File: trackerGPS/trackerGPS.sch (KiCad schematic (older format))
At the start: 0 parts

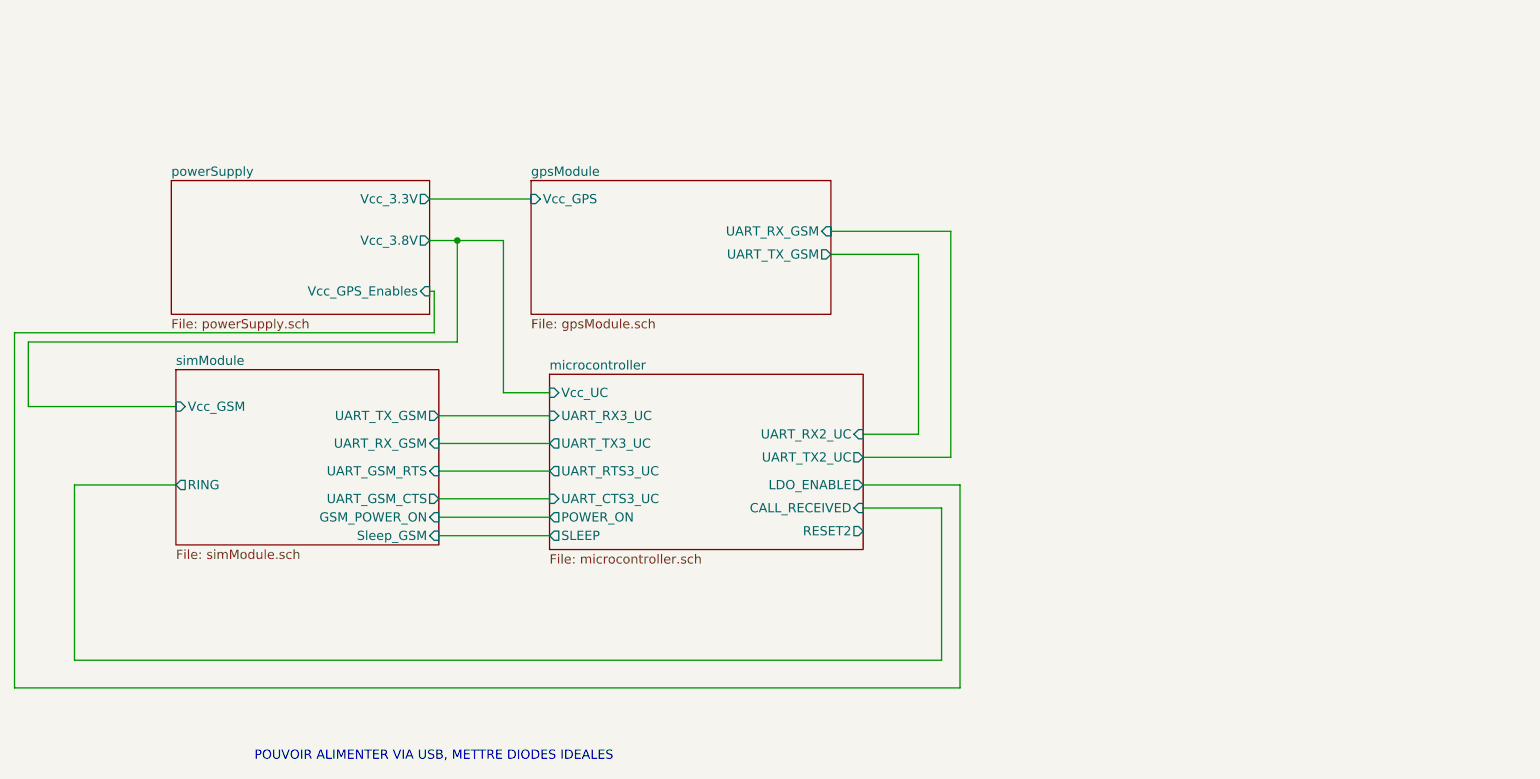
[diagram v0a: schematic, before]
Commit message: Component placed 	modified:   trackerGPS/microcontroller.bak 	modified:   trackerGPS/microcontroller.sch 	modified:   trackerGPS/powerSupply.bak 	modified:   trackerGPS/powerSupply.sch 	modified:   trackerGPS/simModule.bak 	modified:   trackerGPS/simModule.sch 	modified:   trackerGPS/trackerGPS-cache.lib 	modified:   trackerGPS/trackerGPS.bak 	modified:   trackerGPS/trackerGPS.kicad_pcb 	modified:   trackerGPS/trackerGPS.kicad_pcb-bak 	modified:   trackerGPS/trackerGPS.sch
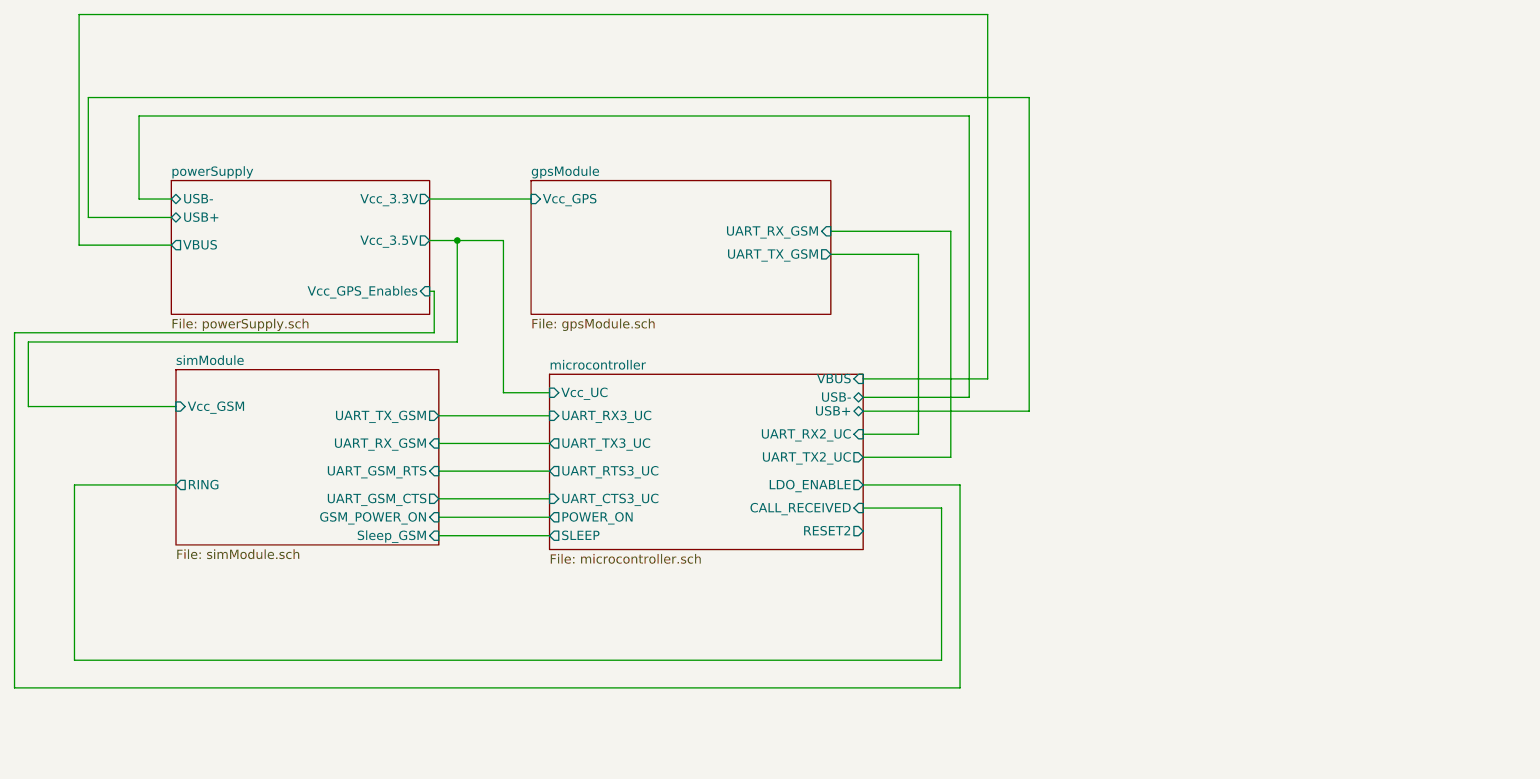
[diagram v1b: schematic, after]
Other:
- note removed: "POUVOIR ALIMENTER VIA USB, METTRE DIODES IDEALES"
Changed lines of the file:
@@
 $EndDescr
-$Sheet
-S 4525 4300 1700 950
-U 6058B695
-F0 "microcontroller" 50
-F1 "microcontroller.sch" 50
-F2 "Vcc_UC" I L 4525 4400 50
-F3 "UART_RX2_UC" I R 6225 4625 50
-F4 "UART_TX2_UC" O R 6225 4750 50
-F5 "UART_RX3_UC" I L 4525 4525 50
-F6 "UART_TX3_UC" O L 4525 4675 50
-F7 "UART_RTS3_UC" O L 4525 4825 50
-F8 "UART_CTS3_UC" I L 4525 4975 50
-F9 "RESET2" O R 6225 5150 50
-F10 "LDO_ENABLE" O R 6225 4900 50
-F11 "CALL_RECEIVED" I R 6225 5025 50
-F12 "POWER_ON" O L 4525 5075 50
-F13 "SLEEP" O L 4525 5175 50
-$EndSheet
 $Sheet
 S 2500 4275 1425 950
@@
 F1 "powerSupply.sch" 50
 F2 "Vcc_3.3V" O R 3875 3350 50
-F3 "Vcc_3.8V" O R 3875 3575 50
-F4 "Vcc_GPS_Enables" I R 3875 3850 50
+F3 "Vcc_GPS_Enables" I R 3875 3850 50
+F4 "USB+" B L 2475 3450 50
+F5 "USB-" B L 2475 3350 50
+F6 "Vcc_3.5V" O R 3875 3575 50
+F7 "VBUS" O L 2475 3600 50
 $EndSheet
 Wire Wire Line
@@
 Wire Wire Line
 	4525 5175 3925 5175
-Text Notes 2925 6400 0    50   ~ 0
-POUVOIR ALIMENTER VIA USB, METTRE DIODES IDEALES
+$Sheet
+S 4525 4300 1700 950
+U 6058B695
+F0 "microcontroller" 50
+F1 "microcontroller.sch" 50
+F2 "Vcc_UC" I L 4525 4400 50
+F3 "UART_RX2_UC" I R 6225 4625 50
+F4 "UART_TX2_UC" O R 6225 4750 50
+F5 "UART_RX3_UC" I L 4525 4525 50
+F6 "UART_TX3_UC" O L 4525 4675 50
+F7 "UART_RTS3_UC" O L 4525 4825 50
+F8 "UART_CTS3_UC" I L 4525 4975 50
+F9 "RESET2" O R 6225 5150 50
+F10 "LDO_ENABLE" O R 6225 4900 50
+F11 "CALL_RECEIVED" I R 6225 5025 50
+F12 "POWER_ON" O L 4525 5075 50
+F13 "SLEEP" O L 4525 5175 50
+F14 "USB+" B R 6225 4500 50
+F15 "USB-" B R 6225 4425 50
+F16 "VBUS" I R 6225 4325 50
+$EndSheet
+Wire Wire Line
+	2475 3600 1975 3600
+Wire Wire Line
+	1975 3600 1975 2350
+Wire Wire Line
+	6225 4500 7125 4500
+Wire Wire Line
+	7125 4500 7125 2800
+Wire Wire Line
+	7125 2800 2025 2800
+Wire Wire Line
+	2025 2800 2025 3450
+Wire Wire Line
+	2025 3450 2475 3450
+Wire Wire Line
+	2475 3350 2300 3350
+Wire Wire Line
+	2300 3350 2300 2900
+Wire Wire Line
+	2300 2900 6800 2900
+Wire Wire Line
+	6800 2900 6800 4425
+Wire Wire Line
+	6800 4425 6225 4425
+Wire Wire Line
+	6225 4325 6900 4325
+Wire Wire Line
+	6900 4325 6900 2350
+Wire Wire Line
+	1975 2350 6900 2350
 $EndSCHEMATC

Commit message: PCB completed with test points 	modified:   trackerGPS/gpsModule.bak 	modified:   trackerGPS/gpsModule.sch 	modified:   trackerGPS/microcontroller.bak 	modified:   trackerGPS/microcontroller.sch 	modified:   trackerGPS/powerSupply.bak 	modified:   trackerGPS/powerSupply.sch 	modified:   trackerGPS/simModule.bak 	modified:   trackerGPS/simModule.sch 	modified:   trackerGPS/trackerGPS-cache.lib 	modified:   trackerGPS/trackerGPS.bak 	modified:   trackerGPS/trackerGPS.kicad_pcb 	modified:   trackerGPS/trackerGPS.kicad_pcb-bak 	modified:   trackerGPS/trackerGPS.sch
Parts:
- added H1, H2, H3, H4: MountingHole_Pad, MountingHole:MountingHole_2.5mm_Pad_Via, symbol Mechanical:MountingHole_Pad
- added R19, R20, R21, R22: 0ohm, Resistor_SMD:R_0805_2012Metric_Pad1.15x1.40mm_HandSolder, symbol Device:R_Small
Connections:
- net gpsModule/UART_RX_GSM: now also R20.2
- net gpsModule/UART_TX_GSM: now also R19.1
- net microcontroller/UART_RX3_UC: now also R22.1
- net microcontroller/UART_TX3_UC: now also R21.2
- new net GND: H1.1, H2.1, H3.1, H4.1
- new net microcontroller/UART_RX2_UC: R19.2
- new net microcontroller/UART_TX2_UC: R20.1
- new net simModule/UART_RX_GSM: R21.1
- new net simModule/UART_TX_GSM: R22.2
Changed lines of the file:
@@
 F2 "UART_RX_GSM" I R 3925 4675 50
 F3 "UART_TX_GSM" O R 3925 4525 50
-F4 "UART_GSM_CTS" O R 3925 4975 50
-F5 "UART_GSM_RTS" I R 3925 4825 50
-F6 "Vcc_GSM" I L 2500 4475 50
-F7 "RING" O L 2500 4900 50
-F8 "Sleep_GSM" I R 3925 5175 50
-F9 "GSM_POWER_ON" I R 3925 5075 50
+F4 "Vcc_GSM" I L 2500 4475 50
+F5 "RING" O L 2500 4900 50
+F6 "Sleep_GSM" I R 3925 5175 50
+F7 "GSM_POWER_ON" I R 3925 5075 50
+F8 "UART_GSM_CTS" O R 3925 4975 50
+F9 "UART_GSM_RTS" I R 3925 4825 50
 $EndSheet
 $Sheet
@@
 	4275 4400 4525 4400
 Wire Wire Line
-	3925 4975 4525 4975
-Wire Wire Line
-	4525 4825 3925 4825
-Wire Wire Line
-	4525 4525 3925 4525
-Wire Wire Line
-	3925 4675 4525 4675
+	4525 4525 4275 4525
+Wire Wire Line
+	3925 4675 3950 4675
 Wire Wire Line
 	6225 4625 6525 4625
@@
 	6525 4625 6525 3650
 Wire Wire Line
-	6525 3650 6050 3650
-Wire Wire Line
-	6050 3525 6700 3525
+	6525 3650 6375 3650
+Wire Wire Line
+	6050 3525 6200 3525
 Wire Wire Line
 	6700 3525 6700 4750
@@
 Wire Wire Line
 	1975 2350 6900 2350
+Wire Wire Line
+	4525 4825 3925 4825
+Wire Wire Line
+	3925 4975 4525 4975
+$Comp
+L Mechanical:MountingHole_Pad H2
+U 1 1 606A84B1
+P 7825 4725
+F 0 "H2" H 7925 4776 50  0000 L CNN
+F 1 "MountingHole_Pad" H 7925 4685 50  0000 L CNN
+F 2 "MountingHole:MountingHole_2.5mm_Pad_Via" H 7825 4725 50  0001 C CNN
+F 3 "~" H 7825 4725 50  0001 C CNN
+	1    7825 4725
+	1    0    0    -1
+$EndComp
+$Comp
+L Mechanical:MountingHole_Pad H3
+U 1 1 606A852E
+P 8875 4725
+F 0 "H3" H 8975 4776 50  0000 L CNN
+F 1 "MountingHole_Pad" H 8975 4685 50  0000 L CNN
+F 2 "MountingHole:MountingHole_2.5mm_Pad_Via" H 8875 4725 50  0001 C CNN
+F 3 "~" H 8875 4725 50  0001 C CNN
+	1    8875 4725
+	1    0    0    -1
+$EndComp
+$Comp
+L Mechanical:MountingHole_Pad H1
+U 1 1 606A8550
+P 7800 5325
+F 0 "H1" H 7900 5376 50  0000 L CNN
+F 1 "MountingHole_Pad" H 7900 5285 50  0000 L CNN
+F 2 "MountingHole:MountingHole_2.5mm_Pad_Via" H 7800 5325 50  0001 C CNN
+F 3 "~" H 7800 5325 50  0001 C CNN
+	1    7800 5325
+	1    0    0    -1
+$EndComp
+$Comp
+L Mechanical:MountingHole_Pad H4
+U 1 1 606A8581
+P 8900 5350
+F 0 "H4" H 9000 5401 50  0000 L CNN
+F 1 "MountingHole_Pad" H 9000 5310 50  0000 L CNN
+F 2 "MountingHole:MountingHole_2.5mm_Pad_Via" H 8900 5350 50  0001 C CNN
+F 3 "~" H 8900 5350 50  0001 C CNN
+	1    8900 5350
+	1    0    0    -1
+$EndComp
+$Comp
+L power:GND #PWR0156
+U 1 1 606A91CE
+P 7800 5550
+F 0 "#PWR0156" H 7800 5300 50  0001 C CNN
+F 1 "GND" H 7805 5377 50  0000 C CNN
+F 2 "" H 7800 5550 50  0001 C CNN
+F 3 "" H 7800 5550 50  0001 C CNN
+	1    7800 5550
+	1    0    0    -1
+$EndComp
+$Comp
+L power:GND #PWR0157
+U 1 1 606A91F4
+P 8900 5575
+F 0 "#PWR0157" H 8900 5325 50  0001 C CNN
+F 1 "GND" H 8905 5402 50  0000 C CNN
+F 2 "" H 8900 5575 50  0001 C CNN
+F 3 "" H 8900 5575 50  0001 C CNN
+	1    8900 5575
+	1    0    0    -1
+$EndComp
+$Comp
+L power:GND #PWR0158
+U 1 1 606A9207
+P 8875 4925
+F 0 "#PWR0158" H 8875 4675 50  0001 C CNN
+F 1 "GND" H 8880 4752 50  0000 C CNN
+F 2 "" H 8875 4925 50  0001 C CNN
+F 3 "" H 8875 4925 50  0001 C CNN
+	1    8875 4925
+	1    0    0    -1
+$EndComp
+$Comp
+L power:GND #PWR0159
+U 1 1 606A921E
+P 7825 4950
+F 0 "#PWR0159" H 7825 4700 50  0001 C CNN
+F 1 "GND" H 7830 4777 50  0000 C CNN
+F 2 "" H 7825 4950 50  0001 C CNN
+F 3 "" H 7825 4950 50  0001 C CNN
+	1    7825 4950
+	1    0    0    -1
+$EndComp
+Wire Wire Line
+	8875 4825 8875 4925
+Wire Wire Line
+	7825 4825 7825 4950
+Wire Wire Line
+	7800 5425 7800 5550
+Wire Wire Line
+	8900 5450 8900 5575
+Wire Wire Line
+	6400 3525 6700 3525
+Wire Wire Line
+	6175 3650 6050 3650
+$Comp
+L Device:R_Small R20
+U 1 1 606B1DEA
+P 6300 3525
+F 0 "R20" V 6104 3525 50  0000 C CNN
+F 1 "0ohm" V 6195 3525 50  0000 C CNN
+F 2 "Resistor_SMD:R_0805_2012Metric_Pad1.15x1.40mm_HandSolder" H 6300 3525 50  0001 C CNN
+F 3 "~" H 6300 3525 50  0001 C CNN
+	1    6300 3525
+	0    1    1    0
+$EndComp
+$Comp
+L Device:R_Small R19
+U 1 1 606B1E7C
+P 6275 3650
+F 0 "R19" V 6200 3650 50  0000 C CNN
+F 1 "0ohm" V 6125 3675 50  0000 C CNN
+F 2 "Resistor_SMD:R_0805_2012Metric_Pad1.15x1.40mm_HandSolder" H 6275 3650 50  0001 C CNN
+F 3 "~" H 6275 3650 50  0001 C CNN
+	1    6275 3650
+	0    -1   -1   0
+$EndComp
+$Comp
+L Device:R_Small R21
+U 1 1 606B3890
+P 4050 4675
+F 0 "R21" V 3975 4675 50  0000 C CNN
+F 1 "0ohm" V 3975 4500 50  0000 C CNN
+F 2 "Resistor_SMD:R_0805_2012Metric_Pad1.15x1.40mm_HandSolder" H 4050 4675 50  0001 C CNN
+F 3 "~" H 4050 4675 50  0001 C CNN
+	1    4050 4675
+	0    -1   -1   0
+$EndComp
+$Comp
+L Device:R_Small R22
+U 1 1 606B38DA
+P 4175 4525
+F 0 "R22" V 3979 4525 50  0000 C CNN
+F 1 "0ohm" V 4070 4525 50  0000 C CNN
+F 2 "Resistor_SMD:R_0805_2012Metric_Pad1.15x1.40mm_HandSolder" H 4175 4525 50  0001 C CNN
+F 3 "~" H 4175 4525 50  0001 C CNN
+	1    4175 4525
+	0    1    1    0
+$EndComp
+Wire Wire Line
+	4075 4525 3925 4525
+Wire Wire Line
+	4150 4675 4525 4675
 $EndSCHEMATC

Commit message: Replaced TLV75201 by REG113NA 	modified:   "Bilan energ\303\251tique tracker GPS.xlsx" 	modified:   trackerGPS/microcontroller.bak 	modified:   trackerGPS/powerSupply.bak 	modified:   trackerGPS/powerSupply.sch 	modified:   trackerGPS/trackerGPS-cache.lib 	modified:   trackerGPS/trackerGPS.bak 	modified:   trackerGPS/trackerGPS.kicad_pcb 	modified:   trackerGPS/trackerGPS.kicad_pcb-bak 	modified:   trackerGPS/trackerGPS.sch
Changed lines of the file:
@@
 F0 "powerSupply" 50
 F1 "powerSupply.sch" 50
-F2 "Vcc_3.3V" O R 3875 3350 50
-F3 "Vcc_GPS_Enables" I R 3875 3850 50
-F4 "USB+" B L 2475 3450 50
-F5 "USB-" B L 2475 3350 50
-F6 "Vcc_3.5V" O R 3875 3575 50
-F7 "VBUS" O L 2475 3600 50
+F2 "Vcc_GPS_Enables" I R 3875 3850 50
+F3 "USB+" B L 2475 3450 50
+F4 "USB-" B L 2475 3350 50
+F5 "VBUS" O L 2475 3600 50
+F6 "Vcc_3.3V_GPS" O R 3875 3350 50
+F7 "Vcc_3.3V_UC" O R 3875 3475 50
+F9 "Vcc_BAT_GSM" O R 3875 3650 50
 $EndSheet
 Wire Wire Line
 	3875 3350 4425 3350
 Wire Wire Line
-	3875 3575 4025 3575
-Wire Wire Line
-	4275 3575 4275 4400
-Wire Wire Line
 	4275 4400 4525 4400
 Wire Wire Line
@@
 	3900 4075 1625 4075
 Wire Wire Line
-	4025 3575 4025 4125
-Wire Wire Line
 	4025 4125 1700 4125
-Connection ~ 4025 3575
-Wire Wire Line
-	4025 3575 4275 3575
 Wire Wire Line
 	1625 6000 6750 6000
@@
 Wire Wire Line
 	4150 4675 4525 4675
+Wire Wire Line
+	3875 3475 4275 3475
+Wire Wire Line
+	4275 3475 4275 4400
+Wire Wire Line
+	3875 3650 4025 3650
+Wire Wire Line
+	4025 3650 4025 4125
 $EndSCHEMATC
